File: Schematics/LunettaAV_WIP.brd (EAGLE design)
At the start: 42 parts, among them IC1 4046N, IC2 4094N, IC3 TLC339P, IC4 7805T, IC5 4051N, IC6 4017N, IC7 4046N, U1 LM358

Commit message: scehmatics fixes
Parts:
- removed CLOCKDIV: (no value), adafruit:1X06
- removed INH: 4040N, 40xx:DIL16
- removed PLLCLOCK: (no value), jumper:JP1
- removed TNSY5VIN: (no value), SparkFun-Retired:1X02
- removed TNSYIN: (no value), jumper:JP4Q
- added D1, D2: 1N4148, diode:DO35-10
- added IC8: 4046N, 40xx:DIL16
- added IC9: 40106N, 40xx:DIL14
- added JP4: (no value), adafruit:2X04
- added JP5: (no value), pinhead:2X08
- added JP6: (no value), pinhead:1X04
- added R18, R19, R20: 100K, MusicThingModular:7MM_RESISTOR
- added R21: (no value), MusicThingModular:7MM_RESISTOR
- added R22: 1K, MusicThingModular:7MM_RESISTOR
- added VR3: 100K, MusicThingModular:9MM_SNAP-IN_POT
- IC1: value 4046N -> TLC339P; device 40xx:DIL16 -> linear:DIL14
- IC2: value 4094N -> 7805T; device 40xx:DIL16 -> linear:TO220H
- IC3: value TLC339P -> 4046N; device linear:DIL14 -> 40xx:DIL16
- IC4: value 7805T -> 4040N; device linear:TO220H -> 40xx:DIL16
- IC5: value 4051N -> 4017N
- IC6: value 4017N -> 4051N
- IC7: value 4046N -> 4094N
- JP1: device jumper:JP8Q -> adafruit:2X04
- JP2: device jumper:JP5Q -> pinhead:1X02
- JP3: device jumper:JP4 -> pinhead:2X06
- R1, R2: value 4.7K -> 10K; device MusicThingModular:10MM_RESISTOR -> MusicThingModular:7MM_RESISTOR
- R12: value 10K -> 100K
- R17: value 10K -> 1K
- R3: value 1K -> 10K; device MusicThingModular:10MM_RESISTOR -> MusicThingModular:7MM_RESISTOR
- R5: value 10K -> 1K; device MusicThingModular:7MM_RESISTOR -> MusicThingModular:10MM_RESISTOR
- R6, R9: value 10K -> 4.7K; device MusicThingModular:7MM_RESISTOR -> MusicThingModular:10MM_RESISTOR
- moved JP1 232.3 mm to (-119.4, -73.7)
- moved JP2 224.6 mm to (-123.2, -116.8), turned to 0 degrees
- moved JP3 212.8 mm to (-116.8, -96.5)
- moved R16 181.9 mm to (-120.7, -66.0)
- moved R17 180.7 mm to (-120.7, -31.8)
- moved R15 180.2 mm to (-120.7, -62.2)
- moved R14 179.2 mm to (-120.7, -58.4)
- moved R13 178.8 mm to (-120.7, -54.6)
- moved IC2 80.1 mm to (7.62, 38.1)
- moved IC4 62.2 mm to (69.8, 38.1)
- moved R10 58.6 mm to (-86.4, 108.0)
- moved R11 58.6 mm to (-96.5, 108.0)
- moved R6 57.2 mm to (-19.1, 109.2)
- moved IC7 49.5 mm to (87.6, 41.9)
- moved R8 48.5 mm to (-48.3, 113.0)
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- renumbered ERASE to S3, OFFSET to S1, OLED1 to DISP$1, OLED2 to DISP$2, SCALER to VR2, SPEEDER to VR1, TEENSY to B1, WRITE to S2
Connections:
- removed net MINH: IC5.6, JP3.1, R14.1
- removed net PLL/64: CLOCKDIV.6, INH.2
- new net DRONEOUT: R20.1, VR3.2
- new net GATEIN: JP6.4, R18.1
- new net MELODYBUFF: D1.C, VR3.3
- new net MIX: R19.2, R20.2, R21.2
- new net N$11: IC6.6, R13.2
- new net N$7: D1.A, D2.A, R18.2
- new net N$8: R22.2, S2.1
- new net VCAOUT: D2.C, R19.1
- net 3V3: now also R10.2, R11.2, R4.2, R9.2; no longer R1.2, R2.2, R5.2, R8.2
- net 5V: now also IC1.10, IC1.4, IC1.6, IC1.8, IC2.3, JP2.1; no longer IC3.10, IC3.4, IC3.6, IC3.8, IC4.3, TNSY5VIN.1
- net 9V: now also IC1.3, IC3.16, IC4.16, IC6.16, IC7.1, IC7.15, IC8.16, R22.1; no longer IC1.16, IC2.16, IC3.3, IC4.1, IC5.16, INH.16, S2.1
- net AUDIORATE: now also IC5.14; no longer IC6.14
- net BUFFCLOCK: now also IC7.3; no longer IC2.3
- net CLOCKSELECT: now also JP4.2, JP4.4, JP4.6, JP4.8; no longer JP2.1, JP2.3, JP2.5, JP2.7, JP2.9
- net DIN1: now also R5.2; no longer R3.2
- net GND: now also IC1.12, IC2.2, IC3.5, IC3.8, IC4.8, IC6.7, IC6.8, IC8.8, R1.1, R13.1, R14.1, R15.1, R16.1, R2.1, R21.1, R5.1, R8.1, VR3.1; no longer IC1.8, IC2.8, IC3.12, IC4.2, IC5.7, IC5.8, IC7.5, INH.8, R10.1, R11.1, R14.2, R15.2, R16.2, R17.2, R4.1, R9.1
- net MELODYOUT: now also IC5.3; no longer IC6.3
- net MOOX: now also IC6.9, JP6.1, R16.2; no longer IC5.9, JP3.4, R17.1
- net MOXO: now also IC6.10, JP6.2, R15.2; no longer IC5.10, JP3.3, R16.1
- net MXOO: now also IC6.11, JP6.3, R14.2; no longer IC5.11, JP3.2, R15.1
- net N$1: now also JP2.2; no longer TNSY5VIN.2
- net N$19: now also IC5.15, IC6.3; no longer IC5.3, IC6.15
- net N$2: now also IC3.7; no longer IC7.7
- net N$20: now also IC5.4, IC6.13; no longer IC5.13, IC6.4
- net N$21: now also IC5.7, IC6.14; no longer IC5.14, IC6.7
- net N$22: now also IC5.10, IC6.15; no longer IC5.15, IC6.10
- net N$23: now also IC5.1, IC6.12; no longer IC5.12, IC6.1
- net N$24: now also IC5.5, IC6.1; no longer IC5.1, IC6.5
- net N$25: now also IC5.6, IC6.5; no longer IC5.5, IC6.6
- net N$26: now also IC5.9, IC6.2; no longer IC5.2, IC6.9
- net N$27: now also IC5.11, IC6.4; no longer IC5.4, IC6.11
- net N$28: now also IC7.2, R17.1; no longer IC2.2, R13.1
- net N$3: now also R6.1; no longer R1.1
- net N$4: now also R9.1; no longer R2.1
- net N$5: now also IC3.6; no longer IC7.6
- net N$6: now also IC3.11, R12.2; no longer IC7.11, R4.2
- net OOX: now also IC1.11, JP1.1, JP1.2, R8.2; no longer IC3.11, R12.2, TNSYIN.1, TNSYIN.2
- net OXO: now also IC1.9, JP1.3, JP1.4, R3.2; no longer IC3.9, R11.2, TNSYIN.3, TNSYIN.4
- net PLL/16: now also IC4.5, JP3.10, JP3.9; no longer CLOCKDIV.4, INH.5, JP2.2
- net PLL/2: now also IC4.9, JP3.3, JP3.4, JP4.3; no longer CLOCKDIV.1, INH.9, JP2.8
- net PLL/32: now also IC4.3, JP3.11, JP3.12; no longer CLOCKDIV.5, INH.3
- net PLL/4: now also IC4.7, JP3.5, JP3.6, JP4.5; no longer CLOCKDIV.2, INH.7, JP2.6
- net PLL/8: now also IC4.6, JP3.7, JP3.8, JP4.7; no longer CLOCKDIV.3, INH.6, JP2.4
- net PLLCLOCKOUT: now also IC3.4, IC4.10, JP3.1, JP3.2, JP4.1; no longer IC7.4, INH.10, JP2.10, PLLCLOCK.1, PLLCLOCK.2
- net RESET: now also IC1.5, JP1.7, JP1.8, R1.2; no longer IC3.5, R9.2, TNSYIN.7, TNSYIN.8
- net SPEEDYBUFF: now also IC3.9; no longer IC7.9
- net SR1: now also IC7.4, JP5.1, JP5.2; no longer IC2.4, JP1.1, JP1.2
- net SR2: now also IC7.5, JP5.3, JP5.4; no longer IC2.5, JP1.3, JP1.4
- net SR3: now also IC7.6, JP5.5, JP5.6; no longer IC2.6, JP1.5, JP1.6
- net SR4: now also IC7.7, JP5.7, JP5.8; no longer IC2.7, JP1.7, JP1.8
- net SR5: now also IC7.14, JP5.10, JP5.9; no longer IC2.14, JP1.10, JP1.9
- net SR6: now also IC7.13, JP5.11, JP5.12; no longer IC2.13, JP1.11, JP1.12
- net SR7: now also IC7.12, JP5.13, JP5.14; no longer IC2.12, JP1.13, JP1.14
- net SR8: now also IC7.11, JP5.15, JP5.16, R17.2; no longer IC2.11, JP1.15, JP1.16, R13.2
- net TNSYOOX: now also IC1.13, R11.1; no longer IC3.13, R8.1
- net TNSYOXO: now also IC1.14, R10.1; no longer IC3.14, R7.1
- net TNSYRES: now also IC1.2, R4.1; no longer IC3.2, R5.1
- net TNSYXOO: now also IC1.1, R7.1; no longer IC3.1, R6.1
- net VDD: now also IC5.16, IC9.14; no longer IC6.16
- net VSS: now also IC5.8, IC9.7; no longer IC6.8
- net XOO: now also IC1.7, JP1.5, JP1.6, R2.2; no longer IC3.7, R10.2, TNSYIN.5, TNSYIN.6

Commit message: schematic updates
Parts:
- added C2: .1uF, capacitor-wima:C2.5-2
- added R23: LDR, rcl:0204V
- added VR4: 100K, MusicThingModular:9MM_SNAP-IN_POT
- R21: value (none) -> 10K
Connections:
- removed net MELODYBUFF: D1.C, VR3.3
- new net N$10: IC9.4, IC9.5
- new net N$12: C2.1, IC9.1, R23.2, VR4.2
- new net N$9: IC9.2, IC9.3, R23.1, VR4.1
- net AUDIORATE: now also IC9.6
- net GND: now also C2.2, IC9.11, IC9.13, IC9.9
- net MELODYOUT: now also D1.C, VR3.3
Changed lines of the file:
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@@
 <attribute name="VALUE" x="-117.594409375" y="-25.132128125" size="1.143" layer="27" ratio="10" align="bottom-right"/>
 </element>
-<element name="R21" library="MusicThingModular" package="7MM_RESISTOR" value="" x="-120.65" y="-27.94" smashed="yes">
+<element name="R21" library="MusicThingModular" package="7MM_RESISTOR" value="10K" x="-120.65" y="-27.94" smashed="yes">
 <attribute name="NAME" x="-123.070771875" y="-26.793884375" size="0.889" layer="25" ratio="10" align="top-left"/>
 <attribute name="VALUE" x="-117.594409375" y="-28.942128125" size="1.143" layer="27" ratio="10" align="bottom-right"/>
@@
 <attribute name="NAME" x="-124.340771875" y="-130.933884375" size="0.889" layer="25" ratio="10" align="top-left"/>
 <attribute name="VALUE" x="-118.864409375" y="-133.082128125" size="1.143" layer="27" ratio="10" align="bottom-right"/>
+</element>
+<element name="VR4" library="MusicThingModular" package="9MM_SNAP-IN_POT" value="100K" x="-133.35" y="-124.46" smashed="yes">
+<attribute name="NAME" x="-137.16" y="-121.92" size="1.0668" layer="25"/>
+<attribute name="VALUE" x="-137.16" y="-128.27" size="1.27" layer="27"/>
+</element>
+<element name="C2" library="capacitor-wima" library_urn="urn:adsk.eagle:library:116" package="C2.5-2" package3d_urn="urn:adsk.eagle:package:5415/1" value=".1uF" x="-135.89" y="-137.16" smashed="yes">
+<attribute name="NAME" x="-137.541" y="-135.636" size="1.27" layer="25" ratio="10"/>
+<attribute name="POPULARITY" value="28" x="-135.89" y="-137.16" size="1.778" layer="27" display="off"/>
+<attribute name="VALUE" x="-137.541" y="-139.954" size="1.27" layer="27" ratio="10"/>
+</element>
+<element name="R23" library="rcl" library_urn="urn:adsk.eagle:library:334" package="0204V" package3d_urn="urn:adsk.eagle:package:23495/1" value="LDR" x="-135.89" y="-143.51" smashed="yes">
+<attribute name="NAME" x="-138.0236" y="-142.3416" size="1.27" layer="25" ratio="10"/>
+<attribute name="POPULARITY" value="11" x="-135.89" y="-143.51" size="1.778" layer="27" display="off"/>
+<attribute name="SPICEPREFIX" value="R" x="-135.89" y="-143.51" size="1.778" layer="27" display="off"/>
+<attribute name="VALUE" x="-138.0236" y="-145.8214" size="1.27" layer="27" ratio="10"/>
 </element>
 </elements>
@@
 <contactref element="R15" pad="1"/>
 <contactref element="R14" pad="1"/>
+<contactref element="C2" pad="2"/>
+<contactref element="IC9" pad="11"/>
+<contactref element="IC9" pad="9"/>
+<contactref element="IC9" pad="13"/>
+<wire x1="-115.57" y1="-120.65" x2="-120.65" y2="-120.65" width="0" layer="19" extent="1-1"/>
+<wire x1="-110.49" y1="-120.65" x2="-115.57" y2="-120.65" width="0" layer="19" extent="1-1"/>
+<wire x1="-134.62" y1="-137.16" x2="-120.65" y2="-120.65" width="0" layer="19" extent="1-1"/>
+<wire x1="-124.46" y1="-66.04" x2="-120.65" y2="-120.65" width="0" layer="19" extent="1-1"/>
 <wire x1="-124.46" y1="-62.23" x2="-124.46" y2="-66.04" width="0" layer="19" extent="1-1"/>
 <wire x1="-124.46" y1="-58.42" x2="-124.46" y2="-62.23" width="0" layer="19" extent="1-1"/>
@@
 <signal name="AUDIORATE">
 <contactref element="IC5" pad="14"/>
+<contactref element="IC9" pad="6"/>
+<wire x1="88.9" y1="7.62" x2="-110.49" y2="-128.27" width="0" layer="19" extent="1-1"/>
 </signal>
 <signal name="MELODYOUT">
 <contactref element="IC5" pad="3"/>
+<contactref element="D1" pad="C"/>
+<contactref element="VR3" pad="3"/>
+<wire x1="-110.49" y1="-5.08" x2="-116.88" y2="-15.89" width="0" layer="19" extent="1-1"/>
+<wire x1="88.9" y1="0" x2="-110.49" y2="-5.08" width="0" layer="19" extent="1-1"/>
 </signal>
 <signal name="N$28">
@@
 <wire x1="81.28" y1="38.1" x2="73.56" y2="12.66" width="0" layer="19" extent="1-1"/>
 </signal>
-<signal name="MELODYBUFF">
-<contactref element="D1" pad="C"/>
-<contactref element="VR3" pad="3"/>
-<wire x1="-110.49" y1="-5.08" x2="-116.88" y2="-15.89" width="0" layer="19" extent="1-1"/>
-</signal>
 <signal name="N$7">
 <contactref element="D1" pad="A"/>
@@
 <wire x1="55.78" y1="7.66" x2="-118.11" y2="-132.08" width="0" layer="19" extent="1-1"/>
 </signal>
+<signal name="N$9">
+<contactref element="IC9" pad="2"/>
+<contactref element="IC9" pad="3"/>
+<contactref element="VR4" pad="1"/>
+<contactref element="R23" pad="1"/>
+<wire x1="-118.11" y1="-128.27" x2="-120.65" y2="-128.27" width="0" layer="19" extent="1-1"/>
+<wire x1="-135.85" y1="-131.46" x2="-120.65" y2="-128.27" width="0" layer="19" extent="1-1"/>
+<wire x1="-137.16" y1="-143.51" x2="-135.85" y2="-131.46" width="0" layer="19" extent="1-1"/>
+</signal>
+<signal name="N$10">
+<contactref element="IC9" pad="4"/>
+<contactref element="IC9" pad="5"/>
+<wire x1="-113.03" y1="-128.27" x2="-115.57" y2="-128.27" width="0" layer="19" extent="1-1"/>
+</signal>
+<signal name="N$12">
+<contactref element="IC9" pad="1"/>
+<contactref element="C2" pad="1"/>
+<contactref element="VR4" pad="2"/>
+<contactref element="R23" pad="2"/>
+<wire x1="-133.35" y1="-131.46" x2="-123.19" y2="-128.27" width="0" layer="19" extent="1-1"/>
+<wire x1="-137.16" y1="-137.16" x2="-133.35" y2="-131.46" width="0" layer="19" extent="1-1"/>
+<wire x1="-134.62" y1="-143.51" x2="-137.16" y2="-137.16" width="0" layer="19" extent="1-1"/>
+</signal>
 </signals>

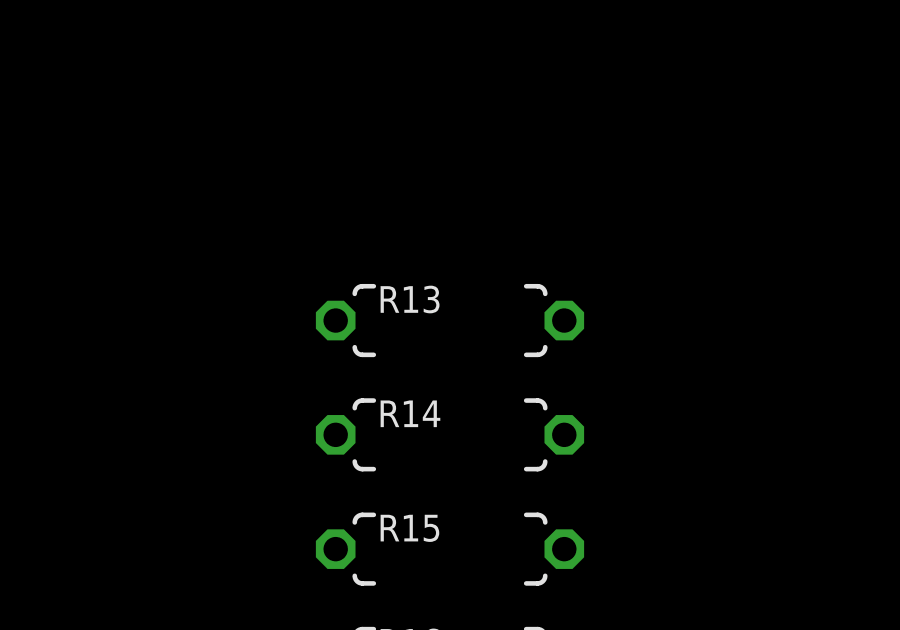
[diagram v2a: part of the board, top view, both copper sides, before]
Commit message: more visuals and functions updated
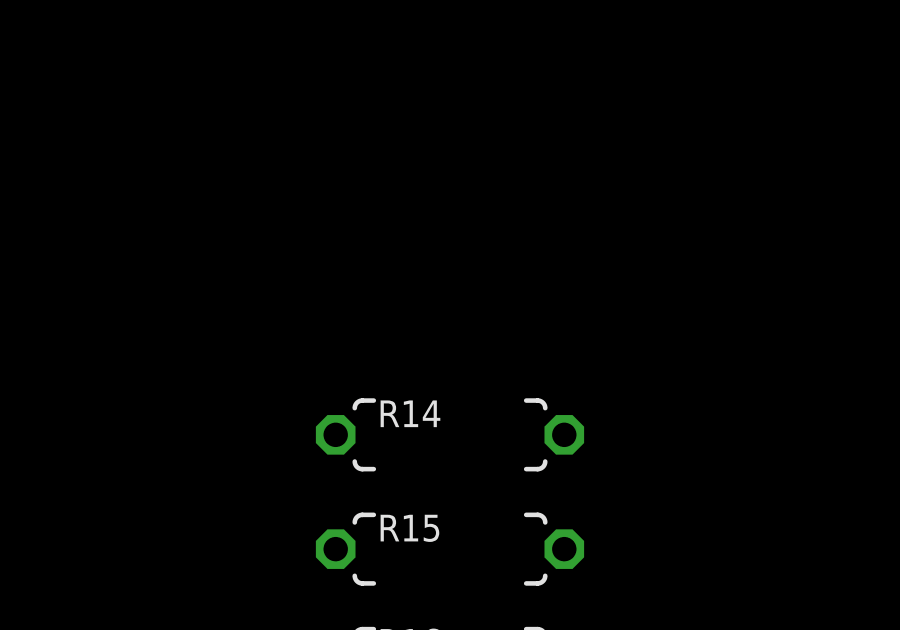
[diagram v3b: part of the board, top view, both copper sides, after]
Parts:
- removed R13: 10K, MusicThingModular:7MM_RESISTOR
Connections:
- removed net N$11 (its old number): IC6.6, R13.2
- net GND: now also IC6.6; no longer R13.1
- net N$9: now also VR4.3; no longer VR4.1
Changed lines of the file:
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@@
 <attribute name="VALUE" x="-117.594409375" y="-32.752128125" size="1.143" layer="27" ratio="10" align="bottom-right"/>
-</element>
-<element name="R13" library="MusicThingModular" package="7MM_RESISTOR" value="10K" x="-120.65" y="-54.61" smashed="yes">
-<attribute name="NAME" x="-123.070771875" y="-53.463884375" size="0.889" layer="25" ratio="10" align="top-left"/>
-<attribute name="VALUE" x="-117.594409375" y="-55.612128125" size="1.143" layer="27" ratio="10" align="bottom-right"/>
 </element>
 <element name="R14" library="MusicThingModular" package="7MM_RESISTOR" value="10K" x="-120.65" y="-58.42" smashed="yes">
@@
 <contactref element="R21" pad="1"/>
 <contactref element="VR3" pad="1"/>
-<contactref element="R13" pad="1"/>
 <contactref element="R16" pad="1"/>
 <contactref element="R15" pad="1"/>
@@
 <contactref element="IC9" pad="9"/>
 <contactref element="IC9" pad="13"/>
+<contactref element="IC6" pad="6"/>
 <wire x1="-115.57" y1="-120.65" x2="-120.65" y2="-120.65" width="0" layer="19" extent="1-1"/>
 <wire x1="-110.49" y1="-120.65" x2="-115.57" y2="-120.65" width="0" layer="19" extent="1-1"/>
@@
 <wire x1="-124.46" y1="-62.23" x2="-124.46" y2="-66.04" width="0" layer="19" extent="1-1"/>
 <wire x1="-124.46" y1="-58.42" x2="-124.46" y2="-62.23" width="0" layer="19" extent="1-1"/>
-<wire x1="-124.46" y1="-54.61" x2="-124.46" y2="-58.42" width="0" layer="19" extent="1-1"/>
-<wire x1="-124.46" y1="-27.94" x2="-124.46" y2="-54.61" width="0" layer="19" extent="1-1"/>
+<wire x1="-124.46" y1="-27.94" x2="-124.46" y2="-58.42" width="0" layer="19" extent="1-1"/>
 <wire x1="-121.88" y1="-15.89" x2="-124.46" y2="-27.94" width="0" layer="19" extent="1-1"/>
 <wire x1="3.85" y1="4.43" x2="-121.88" y2="-15.89" width="0" layer="19" extent="1-1"/>
@@
 <wire x1="96.52" y1="38.1" x2="86.36" y2="52.07" width="0" layer="19" extent="1-1"/>
 <wire x1="78.74" y1="34.29" x2="96.52" y2="38.1" width="0" layer="19" extent="1-1"/>
-<wire x1="99.06" y1="12.7" x2="96.52" y2="38.1" width="0" layer="19" extent="1-1"/>
+<wire x1="96.52" y1="12.7" x2="96.52" y2="38.1" width="0" layer="19" extent="1-1"/>
+<wire x1="99.06" y1="12.7" x2="96.52" y2="12.7" width="0" layer="19" extent="1-1"/>
 <wire x1="101.6" y1="12.7" x2="99.06" y2="12.7" width="0" layer="19" extent="1-1"/>
-<wire x1="73.56" y1="7.66" x2="99.06" y2="12.7" width="0" layer="19" extent="1-1"/>
+<wire x1="73.56" y1="7.66" x2="96.52" y2="12.7" width="0" layer="19" extent="1-1"/>
 <wire x1="-21.59" y1="113.03" x2="3.81" y2="62.23" width="0" layer="19" extent="1-1"/>
 <wire x1="-31.75" y1="113.03" x2="-21.59" y2="113.03" width="0" layer="19" extent="1-1"/>
@@
 <wire x1="96.52" y1="20.32" x2="-116.84" y2="-58.42" width="0" layer="19" extent="1-1"/>
 </signal>
-<signal name="N$11">
-<contactref element="IC6" pad="6"/>
-<contactref element="R13" pad="2"/>
-<wire x1="96.52" y1="12.7" x2="-116.84" y2="-54.61" width="0" layer="19" extent="1-1"/>
-</signal>
 <signal name="PLL/16">
 <contactref element="JP3" pad="10"/>
@@
 <contactref element="IC9" pad="2"/>
 <contactref element="IC9" pad="3"/>
-<contactref element="VR4" pad="1"/>
 <contactref element="R23" pad="1"/>
+<contactref element="VR4" pad="3"/>
 <wire x1="-118.11" y1="-128.27" x2="-120.65" y2="-128.27" width="0" layer="19" extent="1-1"/>
-<wire x1="-135.85" y1="-131.46" x2="-120.65" y2="-128.27" width="0" layer="19" extent="1-1"/>
-<wire x1="-137.16" y1="-143.51" x2="-135.85" y2="-131.46" width="0" layer="19" extent="1-1"/>
+<wire x1="-130.85" y1="-131.46" x2="-120.65" y2="-128.27" width="0" layer="19" extent="1-1"/>
+<wire x1="-137.16" y1="-143.51" x2="-130.85" y2="-131.46" width="0" layer="19" extent="1-1"/>
 </signal>
 <signal name="N$10">
@@
 <wire x1="-113.03" y1="-128.27" x2="-115.57" y2="-128.27" width="0" layer="19" extent="1-1"/>
 </signal>
-<signal name="N$12">
+<signal name="N$11">
 <contactref element="IC9" pad="1"/>
 <contactref element="C2" pad="1"/>

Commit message: fix 4017 schematics
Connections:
- net 9V: now also IC5.16
- net GND: now also IC5.13, IC5.8
- net VDD: no longer IC5.16
- net VSS: no longer IC5.8
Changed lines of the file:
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@@
 </signal>
 <signal name="VSS">
-<contactref element="IC5" pad="8"/>
 <contactref element="IC9" pad="7"/>
-<wire x1="101.6" y1="0" x2="-107.95" y2="-128.27" width="0" layer="19" extent="1-1"/>
 </signal>
 <signal name="VDD">
-<contactref element="IC5" pad="16"/>
 <contactref element="IC9" pad="14"/>
-<wire x1="83.82" y1="7.62" x2="-123.19" y2="-120.65" width="0" layer="19" extent="1-1"/>
 </signal>
 <signal name="GND">
@@
 <contactref element="IC9" pad="13"/>
 <contactref element="IC6" pad="6"/>
+<contactref element="IC5" pad="8"/>
+<contactref element="IC5" pad="13"/>
 <wire x1="-115.57" y1="-120.65" x2="-120.65" y2="-120.65" width="0" layer="19" extent="1-1"/>
 <wire x1="-110.49" y1="-120.65" x2="-115.57" y2="-120.65" width="0" layer="19" extent="1-1"/>
@@
 <wire x1="99.06" y1="12.7" x2="96.52" y2="12.7" width="0" layer="19" extent="1-1"/>
 <wire x1="101.6" y1="12.7" x2="99.06" y2="12.7" width="0" layer="19" extent="1-1"/>
-<wire x1="73.56" y1="7.66" x2="96.52" y2="12.7" width="0" layer="19" extent="1-1"/>
+<wire x1="91.44" y1="7.62" x2="96.52" y2="12.7" width="0" layer="19" extent="1-1"/>
+<wire x1="101.6" y1="0" x2="101.6" y2="12.7" width="0" layer="19" extent="1-1"/>
+<wire x1="73.56" y1="7.66" x2="91.44" y2="7.62" width="0" layer="19" extent="1-1"/>
 <wire x1="-21.59" y1="113.03" x2="3.81" y2="62.23" width="0" layer="19" extent="1-1"/>
 <wire x1="-31.75" y1="113.03" x2="-21.59" y2="113.03" width="0" layer="19" extent="1-1"/>
@@
 <contactref element="IC7" pad="15"/>
 <contactref element="R22" pad="1"/>
+<contactref element="IC5" pad="16"/>
 <wire x1="78.74" y1="45.72" x2="68.58" y2="59.69" width="0" layer="19" extent="1-1"/>
 <wire x1="81.28" y1="45.72" x2="78.74" y2="45.72" width="0" layer="19" extent="1-1"/>
@@
 <wire x1="60.96" y1="41.91" x2="78.74" y2="45.72" width="0" layer="19" extent="1-1"/>
 <wire x1="83.82" y1="20.32" x2="78.74" y2="38.1" width="0" layer="19" extent="1-1"/>
+<wire x1="83.82" y1="7.62" x2="83.82" y2="20.32" width="0" layer="19" extent="1-1"/>
 <wire x1="29.21" y1="44.45" x2="60.96" y2="41.91" width="0" layer="19" extent="1-1"/>
 <wire x1="27.94" y1="49.53" x2="29.21" y2="44.45" width="0" layer="19" extent="1-1"/>
